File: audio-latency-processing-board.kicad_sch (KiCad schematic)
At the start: 0 parts

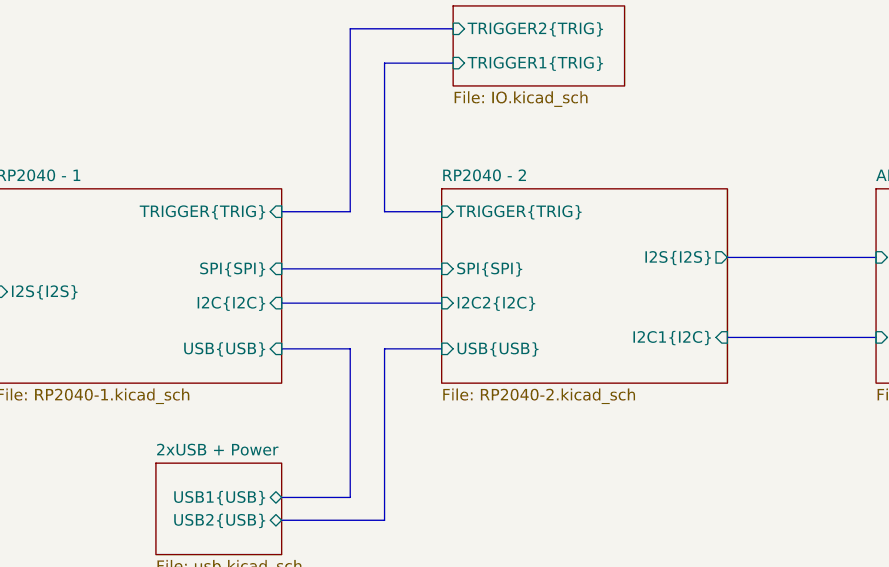
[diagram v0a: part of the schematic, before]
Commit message: [#71555] Fix I2C and SPI channels overlap
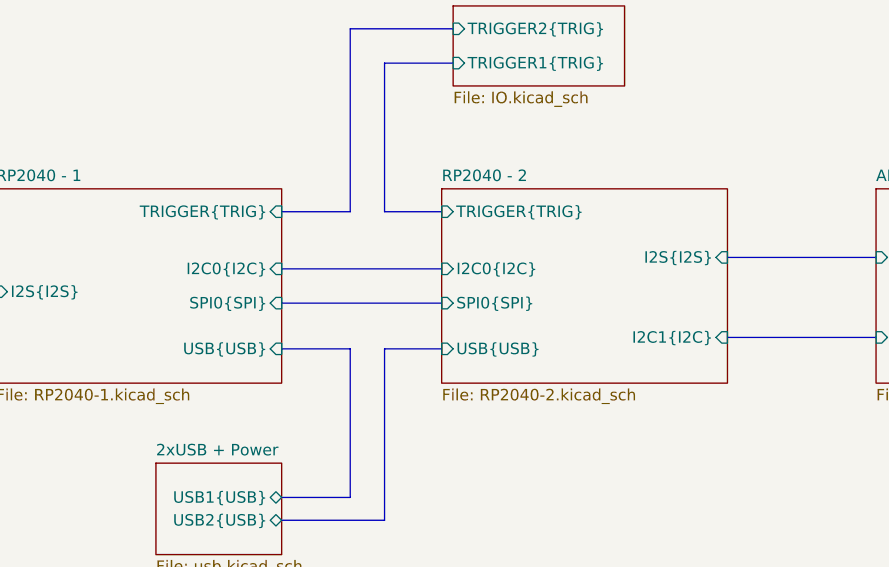
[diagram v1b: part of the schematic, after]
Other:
- sheet RP2040 - 1 ports: added I2C0{I2C}, SPI0{SPI}; removed I2C{I2C}, SPI{SPI}
- sheet RP2040 - 2 ports: added I2C0{I2C}, SPI0{SPI}; removed I2C2{I2C}, SPI{SPI}
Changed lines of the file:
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@@
 	)
 	(bus_alias "SPI"
-		(members "MISO" "MOSI" "SCK" "~{CS1}" "~{CS2}")
+		(members "MISO" "MOSI" "SCK" "~{CS1}" "~{CS0}")
 	)
 	(bus_alias "TRIG"
@@
 			)
 		)
-		(pin "I2C{I2C}" input
-			(at 182.88 133.35 0)
-			(effects
-				(font
-					(size 1.27 1.27)
-				)
-				(justify right)
-			)
-		)
 		(pin "TRIGGER{TRIG}" input
 			(at 182.88 123.19 0)
@@
 			)
 		)
-		(pin "SPI{SPI}" input
-			(at 182.88 129.54 0)
-			(effects
-				(font
-					(size 1.27 1.27)
-				)
-				(justify right)
-			)
-		)
 		(pin "USB{USB}" input
 			(at 182.88 138.43 0)
+			(effects
+				(font
+					(size 1.27 1.27)
+				)
+				(justify right)
+			)
+		)
+		(pin "I2C0{I2C}" input
+			(at 182.88 129.54 0)
+			(effects
+				(font
+					(size 1.27 1.27)
+				)
+				(justify right)
+			)
+		)
+		(pin "SPI0{SPI}" input
+			(at 182.88 133.35 0)
 			(effects
 				(font
@@
 			)
 		)
-		(pin "I2S{I2S}" output
-			(at 232.41 128.27 0)
-			(effects
-				(font
-					(size 1.27 1.27)
-				)
-				(justify right)
-			)
-		)
 		(pin "TRIGGER{TRIG}" input
 			(at 200.66 123.19 180)
@@
 			)
 		)
-		(pin "SPI{SPI}" input
-			(at 200.66 129.54 180)
+		(pin "USB{USB}" input
+			(at 200.66 138.43 180)
 			(effects
 				(font
@@
 			)
 		)
-		(pin "I2C2{I2C}" input
+		(pin "I2S{I2S}" input
+			(at 232.41 128.27 0)
+			(effects
+				(font
+					(size 1.27 1.27)
+				)
+				(justify right)
+			)
+		)
+		(pin "I2C0{I2C}" input
+			(at 200.66 129.54 180)
+			(effects
+				(font
+					(size 1.27 1.27)
+				)
+				(justify left)
+			)
+		)
+		(pin "SPI0{SPI}" input
 			(at 200.66 133.35 180)
 			(effects
 				(font
-					(size 1.27 1.27)
-				)
-				(justify left)
-			)
-		)
-		(pin "USB{USB}" input
-			(at 200.66 138.43 180)
-			(effects
-				(font

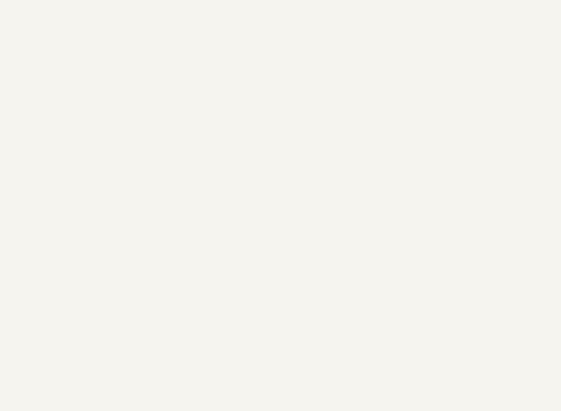
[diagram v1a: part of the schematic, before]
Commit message: [#71555] Add NPTH and change speaker connector to JST XH
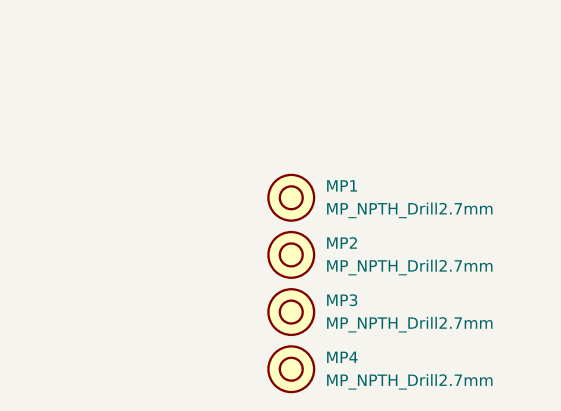
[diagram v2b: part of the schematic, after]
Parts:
- added MP1, MP2, MP3, MP4: MP_NPTH_Drill2.7mm, antmicro-footprints:MP_NPTH_Drill2.7mm, symbol antmicroMechanicalParts:MP_NPTH_Drill2.7mm
